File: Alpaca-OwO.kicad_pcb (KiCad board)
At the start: 4 copper layers, 96 x 45 mm, 43 parts, among them J1 SWD, J2 PS360 ST1, J3 PS360 ST2, J4 Stick, J5 USB_B, J6 Pwny Pr0t, J7 I2C Quick connect, Q1 CJL3415, SW1 Reset, SW2 I2C Pullup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

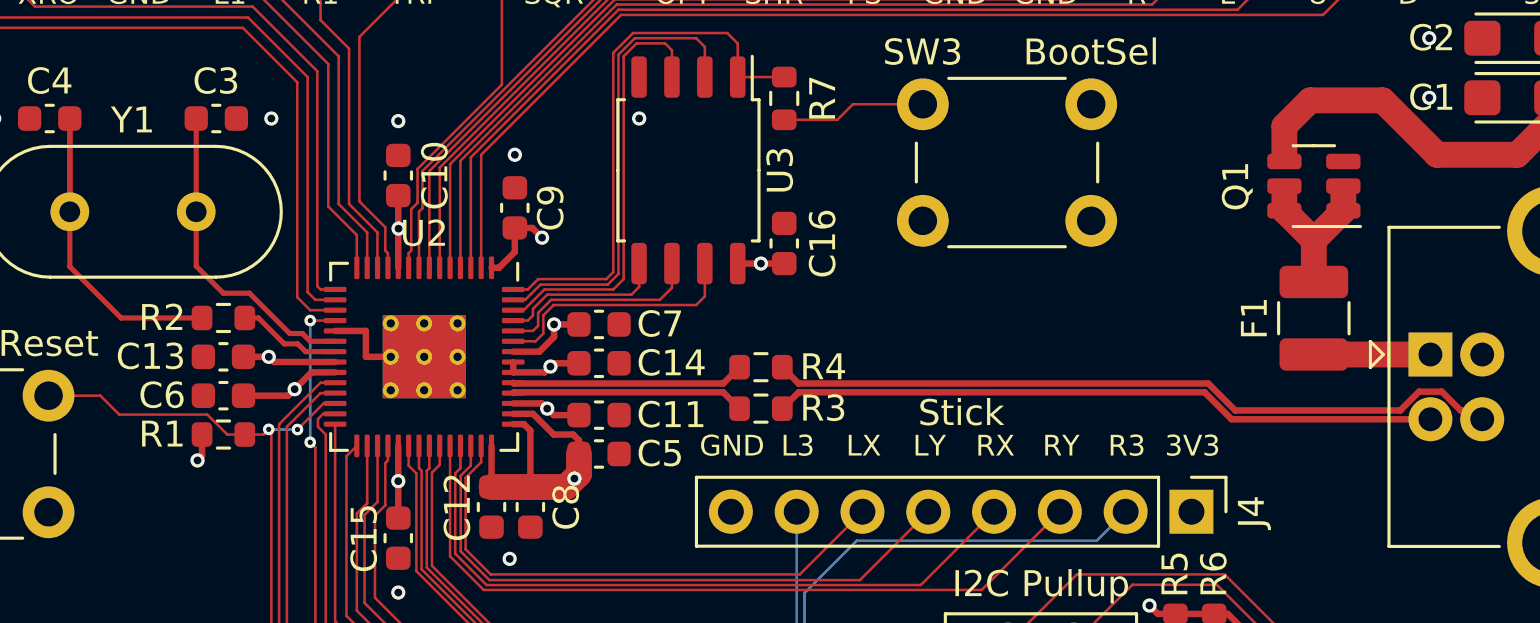
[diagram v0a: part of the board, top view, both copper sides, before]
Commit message: Add more GND vias near components. Update README.
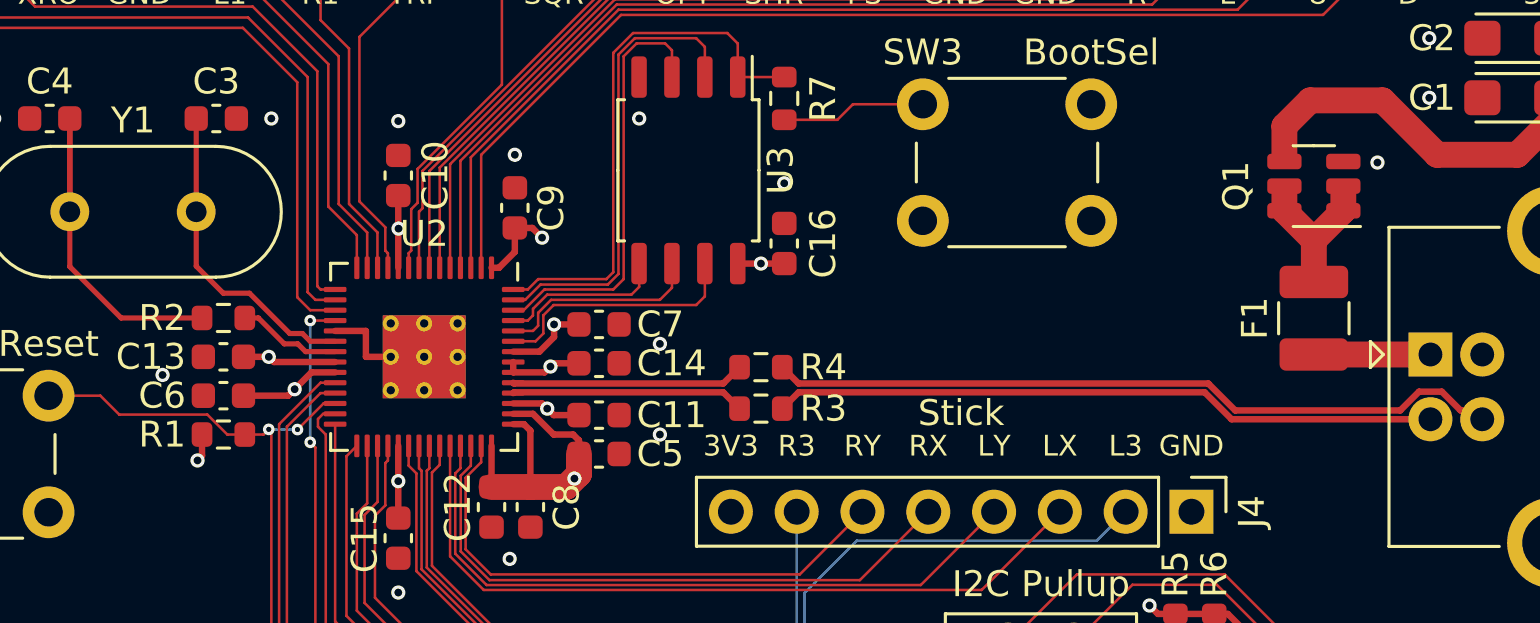
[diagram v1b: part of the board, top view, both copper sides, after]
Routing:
- net GND: vias 12 -> 17
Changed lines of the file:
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@@
     (effects (font (size 1 1) (thickness 0.15)))
   )
-  (gr_text "L3" (at 163.625 105.99) (layer "F.SilkS")
+  (gr_text "L3" (at 176.28 105.99) (layer "F.SilkS")
     (effects (font (size 0.8 0.8) (thickness 0.1)))
   )
@@
     (effects (font (size 0.8 0.8) (thickness 0.1)))
   )
-  (gr_text "RX" (at 171.245 105.99) (layer "F.SilkS")
-    (effects (font (size 0.8 0.8) (thickness 0.1)))
-  )
-  (gr_text "R3" (at 176.325 105.99) (layer "F.SilkS")
+  (gr_text "RX" (at 168.66 105.99) (layer "F.SilkS")
+    (effects (font (size 0.8 0.8) (thickness 0.1)))
+  )
+  (gr_text "R3" (at 163.58 105.99) (layer "F.SilkS")
     (effects (font (size 0.8 0.8) (thickness 0.1)))
   )
@@
     (effects (font (size 0.8 0.8) (thickness 0.1)))
   )
-  (gr_text "3V3" (at 178.865 105.99) (layer "F.SilkS")
+  (gr_text "3V3" (at 161.04 105.99) (layer "F.SilkS")
     (effects (font (size 0.8 0.8) (thickness 0.1)))
   )
@@
     (effects (font (size 0.8 0.8) (thickness 0.1)))
   )
-  (gr_text "RY" (at 173.785 105.99) (layer "F.SilkS")
+  (gr_text "RY" (at 166.12 105.99) (layer "F.SilkS")
     (effects (font (size 0.8 0.8) (thickness 0.1)))
   )
@@
     (effects (font (size 0.8 0.8) (thickness 0.1)))
   )
-  (gr_text "LX" (at 166.165 105.99) (layer "F.SilkS")
+  (gr_text "LX" (at 173.74 105.99) (layer "F.SilkS")
     (effects (font (size 0.8 0.8) (thickness 0.1)))
   )
@@
     (effects (font (size 1 1) (thickness 0.15)) (justify left))
   )
-  (gr_text "GND" (at 161.085 105.99) (layer "F.SilkS")
+  (gr_text "GND" (at 178.82 105.99) (layer "F.SilkS")
     (effects (font (size 0.8 0.8) (thickness 0.1)))
   )
@@
     (effects (font (size 1 1) (thickness 0.15)))
   )
-  (gr_text "LY" (at 168.705 105.99) (layer "F.SilkS")
+  (gr_text "LY" (at 171.2 105.99) (layer "F.SilkS")
     (effects (font (size 0.8 0.8) (thickness 0.1)))
   )
@@
   (via (at 148.2 111.65) (size 0.55) (drill 0.3) (layers "F.Cu" "B.Cu") (free) (net 2))
   (via (at 152.5 110.35) (size 0.55) (drill 0.3) (layers "F.Cu" "B.Cu") (free) (net 2))
+  (via (at 158.3 102.05) (size 0.55) (drill 0.3) (layers "F.Cu" "B.Cu") (free) (net 2))
   (via (at 180.2 118.95) (size 0.55) (drill 0.3) (layers "F.Cu" "B.Cu") (free) (net 2))
   (via (at 188 92.55) (size 0.55) (drill 0.3) (layers "F.Cu" "B.Cu") (net 2))
   (via (at 188 90.25) (size 0.55) (drill 0.3) (layers "F.Cu" "B.Cu") (net 2))
+  (via (at 186 95.05) (size 0.55) (drill 0.3) (layers "F.Cu" "B.Cu") (free) (net 2))
+  (via (at 139.1 103.25) (size 0.55) (drill 0.3) (layers "F.Cu" "B.Cu") (free) (net 2))
   (via (at 148.2 93.45) (size 0.55) (drill 0.3) (layers "F.Cu" "B.Cu") (free) (net 2))
+  (via (at 158.3 105.55) (size 0.55) (drill 0.3) (layers "F.Cu" "B.Cu") (free) (net 2))
   (via (at 157.5 93.35) (size 0.55) (drill 0.3) (layers "F.Cu" "B.Cu") (net 2))
   (via (at 197.6 87.95) (size 0.55) (drill 0.3) (layers "F.Cu" "B.Cu") (free) (net 2))
+  (via (at 163.1 95.85) (size 0.55) (drill 0.3) (layers "F.Cu" "B.Cu") (free) (net 2))
   (via (at 195.6 85.95) (size 0.55) (drill 0.3) (layers "F.Cu" "B.Cu") (free) (net 2))
   (segment (start 140.625 105.55) (end 140.625 106.375) (width 0.25) (layer "F.Cu") (net 3))

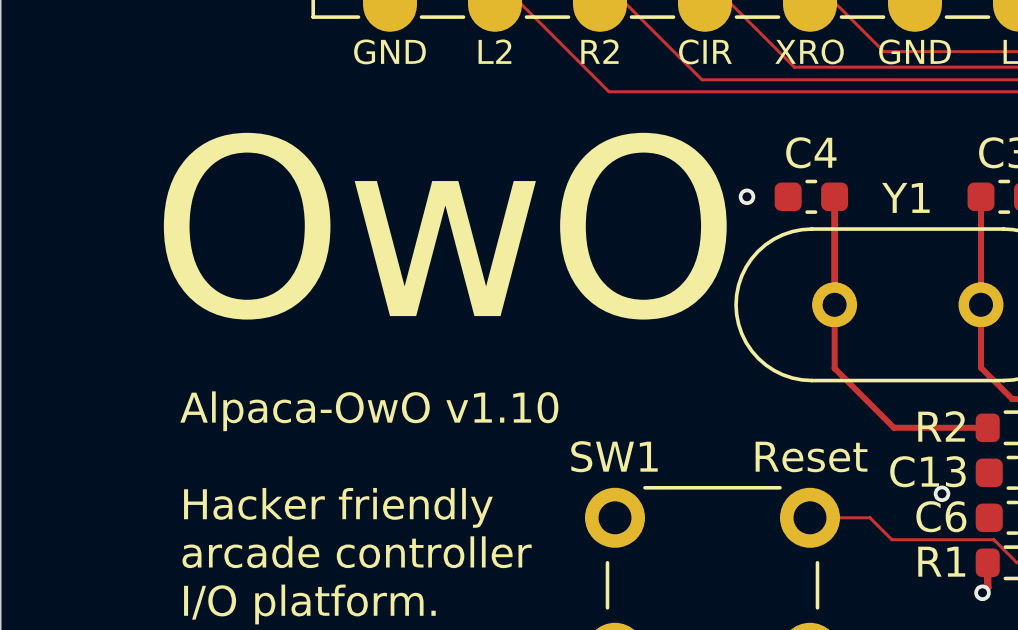
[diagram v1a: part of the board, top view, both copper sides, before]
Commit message: v1.11
Fixed an issue where the analog stick port does not follow the Brook pinout.

No PCB routing was changed but the pin assignment for stick axis and L3/R3 buttons are now mirrored. Refer to README for the new pinout.
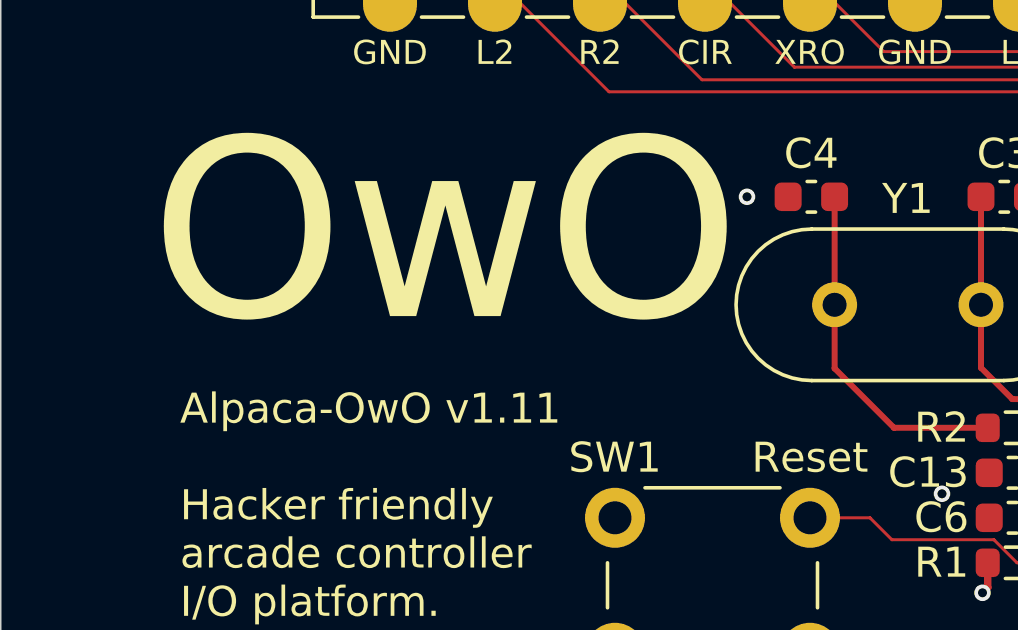
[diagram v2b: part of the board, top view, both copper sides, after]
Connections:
- J4 pad 2: /KEY_L3 -> /KEY_R3
- J4 pad 3: /STK_LX -> /STK_RY
- J4 pad 4: /STK_LY -> /STK_RX
- J4 pad 5: /STK_RX -> /STK_LY
- J4 pad 6: /STK_RY -> /STK_LX
- J4 pad 7: /KEY_R3 -> /KEY_L3
- J6 pad 11: /KEY_L3 -> /KEY_R3
- J6 pad 12: /KEY_R3 -> /KEY_L3
- U2 pad 34: /KEY_L3 -> /KEY_R3
- U2 pad 35: /KEY_R3 -> /KEY_L3
- U2 pad 38: /STK_LX -> /STK_RY
- U2 pad 39: /STK_LY -> /STK_RX
- U2 pad 40: /STK_RX -> /STK_LY
- U2 pad 41: /STK_RY -> /STK_LX
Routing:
- net /KEY_R3: track 30.9 -> 45.8 mm
- net /KEY_L3: track 45.8 -> 30.9 mm
- net /STK_RY: track 21.0 -> 29.6 mm
- net /STK_LX: track 29.6 -> 21.0 mm
- net Net-(C4-Pad2): track 15.4 -> 11.8 mm
- net /STK_RX: track 23.8 -> 26.7 mm
- net /STK_LY: track 26.7 -> 23.8 mm
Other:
- board text added: "Alpaca-OwO v1.11 Hacker friendly arcade controller I/O platform. Proudly based on RP2040"
- board text removed: "Alpaca-OwO v1.10 Hacker friendly arcade controller I/O platform. Proudly based on RP2040"

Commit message: Update silkscreen
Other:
- board text added: "L3 R3"
- board text removed: "R3 L3"
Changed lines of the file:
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@@
     (effects (font (size 1 1) (thickness 0.15)))
   )
-  (gr_text "L3" (at 176.28 105.99) (layer "F.SilkS")
+  (gr_text "L3" (at 163.58 105.99) (layer "F.SilkS")
     (effects (font (size 0.8 0.8) (thickness 0.1)))
   )
-  (gr_text "R3\nL3" (at 159.04 116.15) (layer "F.SilkS")
+  (gr_text "L3\nR3" (at 159.04 116.15) (layer "F.SilkS")
     (effects (font (size 0.8 0.8) (thickness 0.1)))
   )
@@
     (effects (font (size 0.8 0.8) (thickness 0.1)))
   )
-  (gr_text "RX" (at 168.66 105.99) (layer "F.SilkS")
+  (gr_text "RX" (at 171.2 105.99) (layer "F.SilkS")
     (effects (font (size 0.8 0.8) (thickness 0.1)))
   )
-  (gr_text "R3" (at 163.58 105.99) (layer "F.SilkS")
+  (gr_text "R3" (at 176.28 105.99) (layer "F.SilkS")
     (effects (font (size 0.8 0.8) (thickness 0.1)))
   )
@@
     (effects (font (size 0.8 0.8) (thickness 0.1)))
   )
-  (gr_text "RY" (at 166.12 105.99) (layer "F.SilkS")
+  (gr_text "RY" (at 173.74 105.99) (layer "F.SilkS")
     (effects (font (size 0.8 0.8) (thickness 0.1)))
   )
@@
     (effects (font (size 0.8 0.8) (thickness 0.1)))
   )
-  (gr_text "LX" (at 173.74 105.99) (layer "F.SilkS")
+  (gr_text "LX" (at 166.12 105.99) (layer "F.SilkS")
     (effects (font (size 0.8 0.8) (thickness 0.1)))
   )
@@
     (effects (font (size 1 1) (thickness 0.15)))
   )
-  (gr_text "LY" (at 171.2 105.99) (layer "F.SilkS")
+  (gr_text "LY" (at 168.66 105.99) (layer "F.SilkS")
     (effects (font (size 0.8 0.8) (thickness 0.1)))
   )
